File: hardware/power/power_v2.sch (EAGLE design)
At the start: 67 parts, among them J1 12v, J100 FASTON1289_ST, J101 FASTON1289_ST, J2 5v, J3 XT30PW-F, J4 XT30PW-F, J5 XT30PW-F, J6 XT30PW-F, J7 2-PIN, J8 2-PIN, Q1 PSMN1R0-40YSH, Q2 MMBT5401L, Q3 MMBT5401L, Q4 PSMN1R0-40YSH, U1 PDQ30-Q24-S12-D, U2 PDQ30-Q24-S5-D, U3 LM5069_DGS_10, U4 LM5069_DGS_10

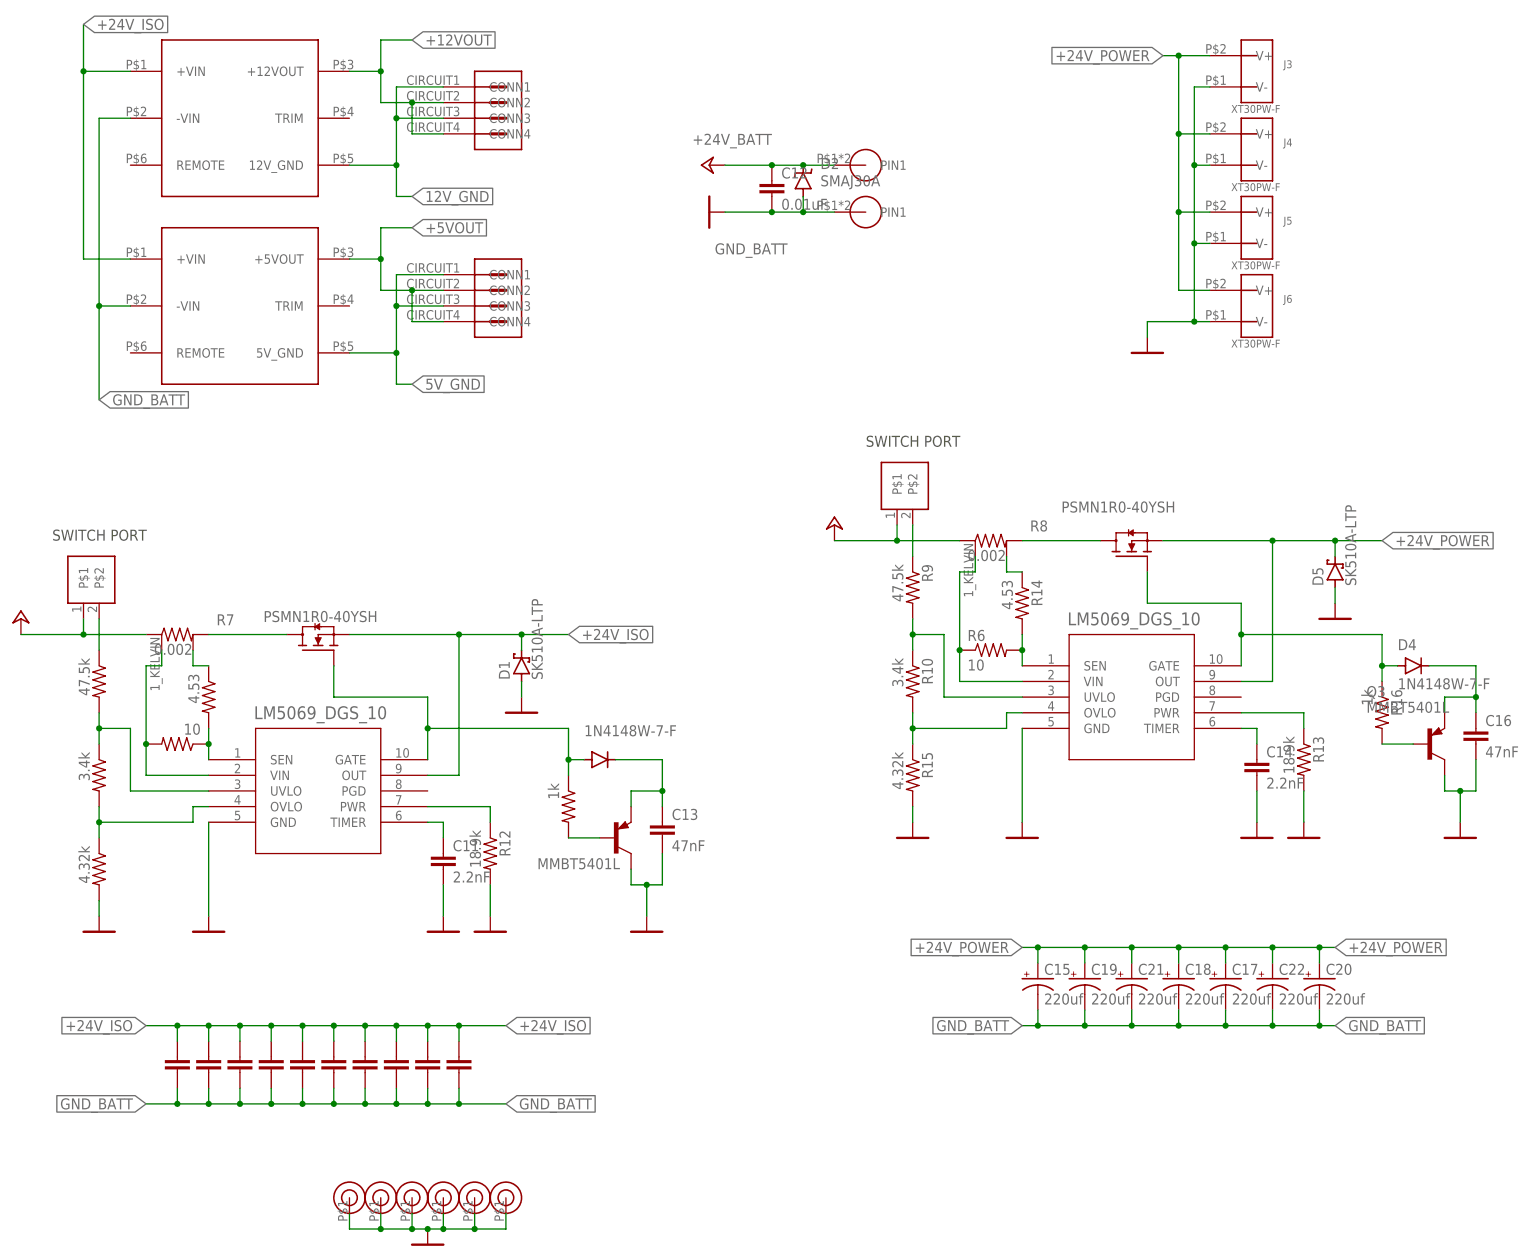
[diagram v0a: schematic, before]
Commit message: Chagned Rpwr
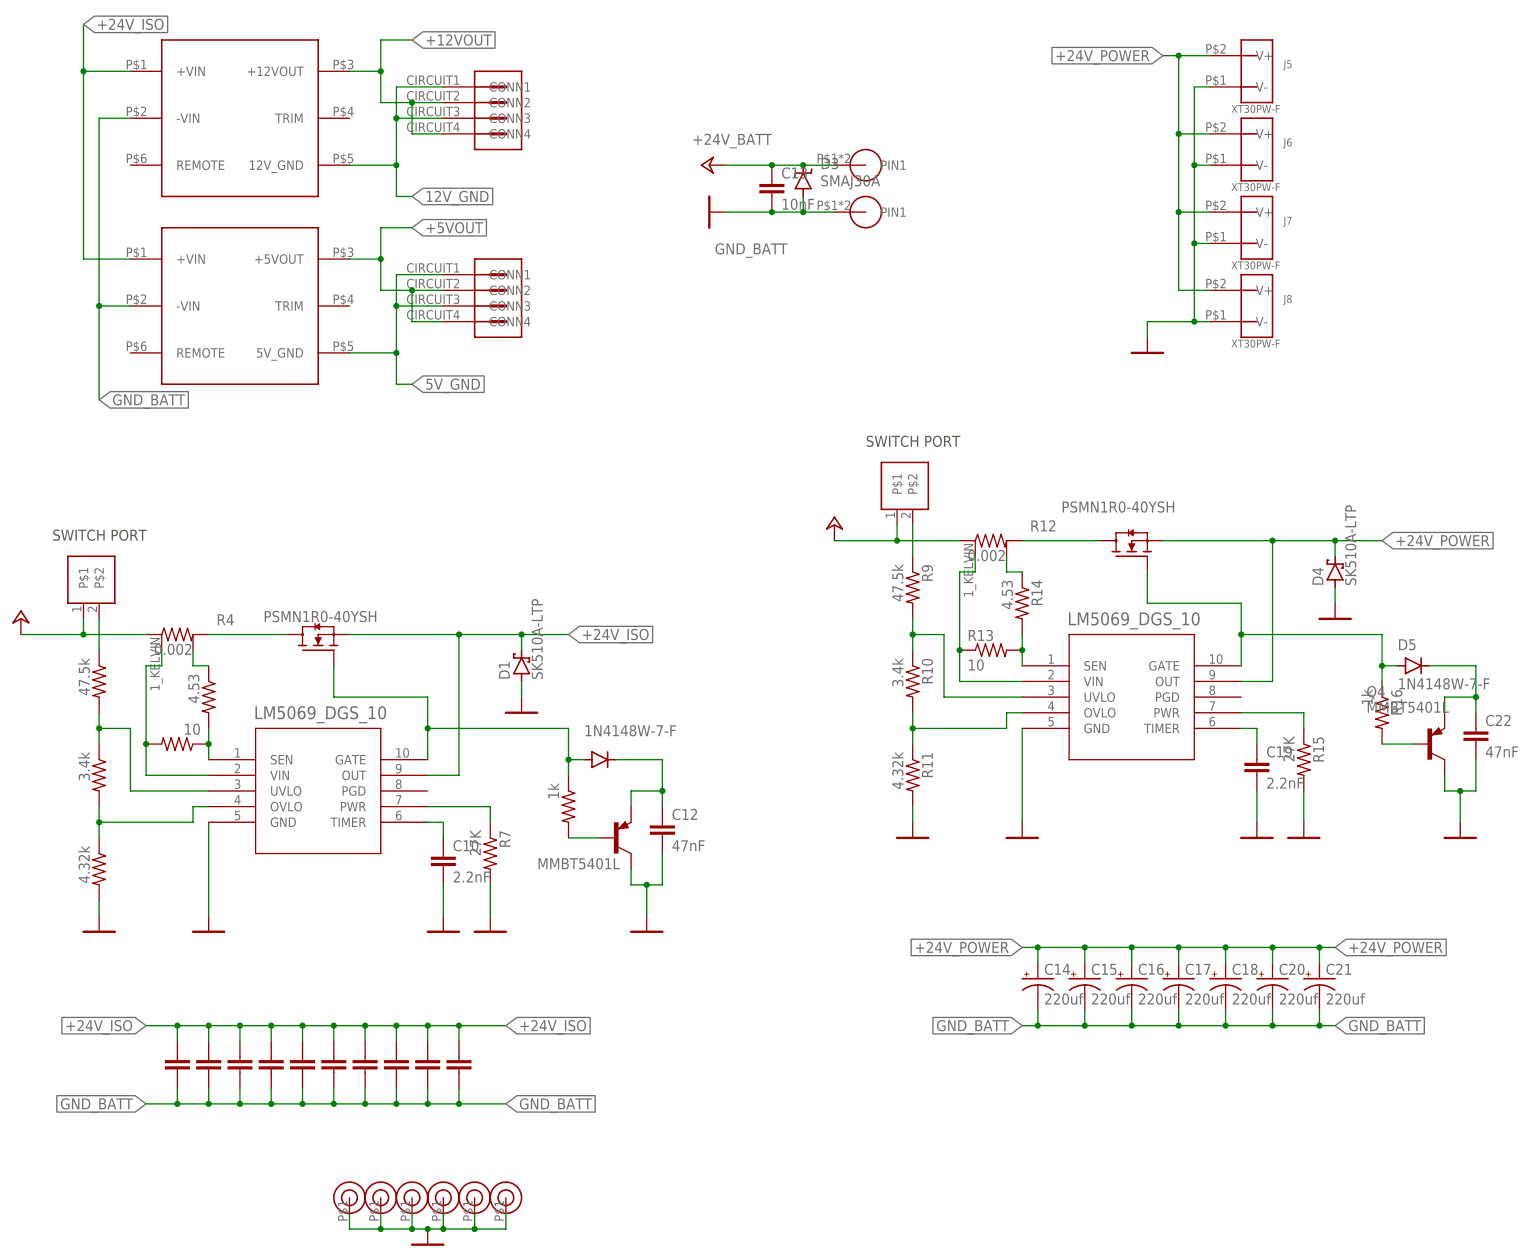
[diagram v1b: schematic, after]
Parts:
- removed U3, U4: LM5069_DGS_10, timlib:LM5069_DGS_10
- added PS3: PDQ30-Q24-S12-D, timlib:PDQ30-Q24-S12-D
- added PS4: PDQ30-Q24-S5-D, timlib:PDQ30-Q24-S5-D
- C1: value 10uF -> 2.2nF
- C10: value 10uF -> 2.2nF; device timlib:C_CERAMIC_1210 -> rcl:C-EUC0603
- C11: value 2.2nF -> 10uF; device rcl:C-EUC0603 -> timlib:C_CERAMIC_1210
- C12: value 0.01uF -> 47nF; device timlib:C_CERAMIC_1210 -> rcl:C-EUC0603
- C13: value 47nF -> 10nF
- C14: value 2.2nF -> 220uf; device rcl:C-EUC0603 -> timlib:35ZLH220MEFC8X11.5
- C16: value 47nF -> 220uf; device rcl:C-EUC0603 -> timlib:35ZLH220MEFC8X11.5
- C19: value 220uf -> 2.2nF; device timlib:35ZLH220MEFC8X11.5 -> rcl:C-EUC0603
- C22: value 220uf -> 47nF; device timlib:35ZLH220MEFC8X11.5 -> rcl:C-EUC0603
- C8: value 2.2nF -> 10uF
- D2: value SMAJ30A -> 1N4148W-7-F; device timlib:SMAJ30A -> timlib:1N4148W-7-F
- D3: value 1N4148W-7-F -> SMAJ30A; device timlib:1N4148W-7-F -> timlib:SMAJ30A
- D4: value 1N4148W-7-F -> SK510A-LTP; device timlib:1N4148W-7-F -> timlib:SK510A-LTP
- D5: value SK510A-LTP -> 1N4148W-7-F; device timlib:SK510A-LTP -> timlib:1N4148W-7-F
- J1: value 12v -> 2-PIN; device timlib:MOLEX_4_RA -> timlib:2-PIN
- J2: value 5v -> 12v
- J3: value XT30PW-F -> 5v; device timlib:XT30PW-F -> timlib:MOLEX_4_RA
- J4: value XT30PW-F -> 2-PIN; device timlib:XT30PW-F -> timlib:2-PIN
- J7, J8: value 2-PIN -> XT30PW-F; device timlib:2-PIN -> timlib:XT30PW-F
- Q3: value MMBT5401L -> PSMN1R0-40YSH; device timlib:MMBT5401L -> timlib:PSMN1R0-40YSH
- Q4: value PSMN1R0-40YSH -> MMBT5401L; device timlib:PSMN1R0-40YSH -> timlib:MMBT5401L
- R1: value 4.32k -> 47.5k
- R11: value 1k -> 4.32k
- R12: value 18.9k -> 0.002; device rcl:R-US_R0603 -> timlib:PMR25HZPFV2L00
- R13: value 18.9k -> 10
- R15: value 4.32k -> 27K
- R3: value 47.5k -> 4.32k
- R4: value 4.53 -> 0.002; device rcl:R-US_R0603 -> timlib:PMR25HZPFV2L00
- R6: value 10 -> 4.53
- R7: value 0.002 -> 27K; device timlib:PMR25HZPFV2L00 -> rcl:R-US_R0603
- R8: value 0.002 -> 1k; device timlib:PMR25HZPFV2L00 -> rcl:R-US_R0603
- U1: value PDQ30-Q24-S12-D -> LM5069_DGS_10; device timlib:PDQ30-Q24-S12-D -> timlib:LM5069_DGS_10
- U2: value PDQ30-Q24-S5-D -> LM5069_DGS_10; device timlib:PDQ30-Q24-S5-D -> timlib:LM5069_DGS_10
- renumbered J100 to P2, J101 to P1
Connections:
- net +12VOUT: now also J2.CONN2, J2.CONN4, PS3.+12VOUT; no longer J1.CONN2, J1.CONN4, U1.+12VOUT
- net +24V_BATT: now also C13.1, D3.C, J1.P$1, J4.P$1, R12.1, R4.1; no longer C12.1, D2.C, J7.P$1, J8.P$1, R7.1, R8.1
- net +24V_ISO: now also C11.1, PS3.+VIN, PS4.+VIN, U1.OUT; no longer C10.1, U1.+VIN, U2.+VIN, U4.OUT
- net +24V_POWER: now also C14.+, C16.+, D4.C, J7.V+, J8.V+, Q3.S, U2.OUT; no longer C19.+, C22.+, D5.C, J3.V+, J4.V+, Q4.S, U3.OUT
- net +5VOUT: now also J3.CONN2, J3.CONN4, PS4.+5VOUT; no longer J2.CONN2, J2.CONN4, U2.+5VOUT
- net 12V_GND: now also J2.CONN1, J2.CONN3, PS3.12V_GND; no longer J1.CONN1, J1.CONN3, U1.12V_GND
- net 5V_GND: now also J3.CONN1, J3.CONN3, PS4.5V_GND; no longer J2.CONN1, J2.CONN3, U2.5V_GND
- net GND_BATT: now also C14.-, C16.-, C19.2, C22.2, D3.A, D4.A, J7.V-, J8.V-, PS3.-VIN, PS4.-VIN, Q4.C, R11.2, R3.2, R7.2, U1.GND, U2.GND; no longer C14.2, C16.2, C19.-, C22.-, D2.A, D5.A, J3.V-, J4.V-, Q3.C, R1.2, R12.2, R13.2, U1.-VIN, U2.-VIN, U3.GND, U4.GND
- net MOSFET_DRAIN: now also Q3.D, R12.2; no longer Q4.D, R8.2
- net MOSFET_DRAIN1: now also R4.2; no longer R7.2
- net N$1: now also U2.UVLO; no longer U3.UVLO
- net N$10: now also R13.2, U2.SEN; no longer R6.2, U3.SEN
- net N$11: now also R12.2K; no longer R8.2K
- net N$12: now also R3.1, U1.OVLO; no longer R1.1, U4.OVLO
- net N$13: now also J1.P$2, R1.1; no longer J7.P$2, R3.1
- net N$14: now also D2.A, R8.1, U1.GATE; no longer D3.A, R11.1, U4.GATE
- net N$15: now also R7.1, U1.PWR; no longer R12.1, U4.PWR
- net N$16: now also C10.1, U1.TIMER; no longer C11.1, U4.TIMER
- net N$17: now also C12.1, D2.C; no longer C13.1, D3.C
- net N$18: now also R8.2; no longer R11.2
- net N$19: now also R12.1K, R13.1, U2.VIN; no longer R6.1, R8.1K, U3.VIN
- net N$2: now also R11.1, U2.OVLO; no longer R15.1, U3.OVLO
- net N$20: now also R6.2, U1.SEN; no longer R4.2, U4.SEN
- net N$21: now also R4.2K, R6.1; no longer R4.1, R7.2K
- net N$22: now also R4.1K, U1.VIN; no longer R7.1K, U4.VIN
- net N$3: now also J4.P$2; no longer J8.P$2
- net N$4: now also R1.2, U1.UVLO; no longer R3.2, U4.UVLO
- net N$5: now also D5.A, Q3.G, U2.GATE; no longer D4.A, Q4.G, U3.GATE
- net N$6: now also R15.1, U2.PWR; no longer R13.1, U3.PWR
- net N$7: now also C19.1, U2.TIMER; no longer C14.1, U3.TIMER
- net N$8: now also C22.1, D5.C, Q4.E; no longer C16.1, D4.C, Q3.E
- net N$9: now also Q4.B; no longer Q3.B
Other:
- moved on the sheet: C12, C13, C15, C17, C18, C20, C21, J5, J6, R13, R15

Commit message: Minor power updates
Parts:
- J1, J4: value 2-PIN -> LINEAR_2_JST_SH_RA; device timlib:2-PIN -> _T_conn:LINEAR_2_JST_SH_RA
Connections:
- net +24V_BATT: now also J1.P1, J4.P1; no longer J1.P$1, J4.P$1
- net N$13: now also J1.P2; no longer J1.P$2
- net N$3: now also J4.P2; no longer J4.P$2
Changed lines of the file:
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@@
 <?xml version="1.0" encoding="utf-8"?>
 <!DOCTYPE eagle SYSTEM "eagle.dtd">
-<eagle version="9.5.2">
+<eagle version="9.6.1">
 <drawing>
 <settings>
@@
 <part name="PS4" library="timlib" library_urn="urn:adsk.eagle:library:16152524" deviceset="PDQ30-Q24-S5-D" device="" package3d_urn="urn:adsk.eagle:package:16187995/4"/>
 <part name="PS3" library="timlib" library_urn="urn:adsk.eagle:library:16152524" deviceset="PDQ30-Q24-S12-D" device="" package3d_urn="urn:adsk.eagle:package:16187995/4"/>
-<part name="J4" library="timlib" library_urn="urn:adsk.eagle:library:16152524" deviceset="2-PIN" device="" package3d_urn="urn:adsk.eagle:package:16399492/4"/>
 <part name="C1" library="timlib" library_urn="urn:adsk.eagle:library:16152524" deviceset="C_CERAMIC" device="_1210" package3d_urn="urn:adsk.eagle:package:23619/2" value="2.2nF"/>
 <part name="C2" library="timlib" library_urn="urn:adsk.eagle:library:16152524" deviceset="C_CERAMIC" device="_1210" package3d_urn="urn:adsk.eagle:package:23619/2" value="10uF"/>
@@
 <part name="U$11" library="timlib" library_urn="urn:adsk.eagle:library:16152524" deviceset="BATT_GND" device="" value="GND_BATT"/>
 <part name="U$12" library="timlib" library_urn="urn:adsk.eagle:library:16152524" deviceset="BATT_GND" device="" value="GND_BATT"/>
-<part name="J1" library="timlib" library_urn="urn:adsk.eagle:library:16152524" deviceset="2-PIN" device="" package3d_urn="urn:adsk.eagle:package:16399492/4"/>
 <part name="U1" library="timlib" library_urn="urn:adsk.eagle:library:16152524" deviceset="LM5069_DGS_10" device="" package3d_urn="urn:adsk.eagle:package:16499421/3"/>
 <part name="P+4" library="timlib" library_urn="urn:adsk.eagle:library:16152524" deviceset="V_BATT" device="" value="+24V_BATT"/>
@@
 <part name="R4" library="timlib" library_urn="urn:adsk.eagle:library:16152524" deviceset="PMR25HZPFV" device="2L00" package3d_urn="urn:adsk.eagle:package:16502583/3" value="0.002"/>
 <part name="R12" library="timlib" library_urn="urn:adsk.eagle:library:16152524" deviceset="PMR25HZPFV" device="2L00" package3d_urn="urn:adsk.eagle:package:16502583/3" value="0.002"/>
-<part name="H1" library="timlib" library_urn="urn:adsk.eagle:library:16152524" deviceset="GND_HOLE" device="_M3" package3d_urn="urn:adsk.eagle:package:19295484/2"/>
-<part name="H2" library="timlib" library_urn="urn:adsk.eagle:library:16152524" deviceset="GND_HOLE" device="_M3" package3d_urn="urn:adsk.eagle:package:19295484/2"/>
-<part name="H3" library="timlib" library_urn="urn:adsk.eagle:library:16152524" deviceset="GND_HOLE" device="_M3" package3d_urn="urn:adsk.eagle:package:19295484/2"/>
-<part name="H4" library="timlib" library_urn="urn:adsk.eagle:library:16152524" deviceset="GND_HOLE" device="_M3" package3d_urn="urn:adsk.eagle:package:19295484/2"/>
-<part name="H5" library="timlib" library_urn="urn:adsk.eagle:library:16152524" deviceset="GND_HOLE" device="_M3" package3d_urn="urn:adsk.eagle:package:19295484/2"/>
-<part name="H6" library="timlib" library_urn="urn:adsk.eagle:library:16152524" deviceset="GND_HOLE" device="_M3" package3d_urn="urn:adsk.eagle:package:19295484/2"/>
+<part name="H1" library="timlib" library_urn="urn:adsk.eagle:library:16152524" deviceset="GND_HOLE" device="_M3" package3d_urn="urn:adsk.eagle:package:19295484/3"/>
+<part name="H2" library="timlib" library_urn="urn:adsk.eagle:library:16152524" deviceset="GND_HOLE" device="_M3" package3d_urn="urn:adsk.eagle:package:19295484/3"/>
+<part name="H3" library="timlib" library_urn="urn:adsk.eagle:library:16152524" deviceset="GND_HOLE" device="_M3" package3d_urn="urn:adsk.eagle:package:19295484/3"/>
+<part name="H4" library="timlib" library_urn="urn:adsk.eagle:library:16152524" deviceset="GND_HOLE" device="_M3" package3d_urn="urn:adsk.eagle:package:19295484/3"/>
+<part name="H5" library="timlib" library_urn="urn:adsk.eagle:library:16152524" deviceset="GND_HOLE" device="_M3" package3d_urn="urn:adsk.eagle:package:19295484/3"/>
+<part name="H6" library="timlib" library_urn="urn:adsk.eagle:library:16152524" deviceset="GND_HOLE" device="_M3" package3d_urn="urn:adsk.eagle:package:19295484/3"/>
 <part name="U$24" library="timlib" library_urn="urn:adsk.eagle:library:16152524" deviceset="BATT_GND" device="" value="GND_BATT"/>
 <part name="C10" library="rcl" library_urn="urn:adsk.eagle:library:334" deviceset="C-EU" device="C0603" package3d_urn="urn:adsk.eagle:package:23616/2" value="2.2nF"/>
@@
 <part name="C12" library="rcl" library_urn="urn:adsk.eagle:library:334" deviceset="C-EU" device="C0603" package3d_urn="urn:adsk.eagle:package:23616/2" value="47nF"/>
 <part name="C22" library="rcl" library_urn="urn:adsk.eagle:library:334" deviceset="C-EU" device="C0603" package3d_urn="urn:adsk.eagle:package:23616/2" value="47nF"/>
+<part name="J1" library="_T_conn" library_urn="urn:adsk.eagle:library:19570503" deviceset="LINEAR_2" device="_JST_SH_RA" package3d_urn="urn:adsk.eagle:package:19570552/2"/>
+<part name="J4" library="_T_conn" library_urn="urn:adsk.eagle:library:19570503" deviceset="LINEAR_2" device="_JST_SH_RA" package3d_urn="urn:adsk.eagle:package:19570552/2"/>
 </parts>
 <sheets>
@@
 </instance>
 <instance part="U$12" gate="G$1" x="200.66" y="152.4" smashed="yes" grouprefs="24V_POWER"/>
-<instance part="J4" gate="G$1" x="162.56" y="124.46" smashed="yes" rot="R90" grouprefs="24V_SOFTSTART"/>
 <instance part="U2" gate="A" x="198.12" y="93.98" smashed="yes" grouprefs="24V_SOFTSTART">
 <attribute name="VALUE" x="187.6806" y="105.6386" size="2.0828" layer="96" ratio="6" rot="SR0"/>
@@
 <instance part="C9" gate="G$1" x="83.82" y="35.56" smashed="yes" grouprefs="ISO_DECOUPLE"/>
 <instance part="C11" gate="G$1" x="88.9" y="35.56" smashed="yes" grouprefs="ISO_DECOUPLE"/>
-<instance part="J1" gate="G$1" x="30.48" y="109.22" smashed="yes" rot="R90" grouprefs="ISO_SOFTSTART"/>
 <instance part="U1" gate="A" x="66.04" y="78.74" smashed="yes" grouprefs="ISO_SOFTSTART">
 <attribute name="VALUE" x="55.6006" y="90.3986" size="2.0828" layer="96" ratio="6" rot="SR0"/>
@@
 <attribute name="VALUE" x="255.524" y="84.201" size="1.778" layer="96"/>
 </instance>
+<instance part="J1" gate="G$1" x="27.94" y="111.76" smashed="yes" rot="R90">
+<attribute name="NAME" x="25.146" y="109.22" size="1.778" layer="95" rot="R90"/>
+<attribute name="VALUE" x="35.56" y="109.22" size="1.778" layer="96" rot="R90"/>
+</instance>
+<instance part="J4" gate="G$1" x="160.02" y="127" smashed="yes" rot="R90">
+<attribute name="NAME" x="157.226" y="124.46" size="1.778" layer="95" rot="R90"/>
+<attribute name="VALUE" x="167.64" y="124.46" size="1.778" layer="96" rot="R90"/>
+</instance>
 </instances>
 <busses>
@@
 <wire x1="170.18" y1="119.38" x2="160.02" y2="119.38" width="0.1524" layer="91" grouprefs="24V_SOFTSTART"/>
 <wire x1="160.02" y1="119.38" x2="149.86" y2="119.38" width="0.1524" layer="91" grouprefs="24V_SOFTSTART"/>
-<pinref part="J4" gate="G$1" pin="P$1"/>
 <wire x1="160.02" y1="121.92" x2="160.02" y2="119.38" width="0.1524" layer="91" grouprefs="24V_SOFTSTART"/>
 <junction x="160.02" y="119.38" grouprefs="24V_SOFTSTART"/>
 <pinref part="R12" gate="G$1" pin="1"/>
+<pinref part="J4" gate="G$1" pin="P1"/>
 </segment>
 <segment>
@@
 <wire x1="27.94" y1="106.68" x2="27.94" y2="104.14" width="0.1524" layer="91" grouprefs="ISO_SOFTSTART"/>
 <junction x="27.94" y="104.14" grouprefs="ISO_SOFTSTART"/>
-<pinref part="J1" gate="G$1" pin="P$1"/>
 <pinref part="P+4" gate="1" pin="+24V"/>
 <pinref part="R4" gate="G$1" pin="1"/>
+<pinref part="J1" gate="G$1" pin="P1"/>
 </segment>
 </net>
@@
 <net name="N$3" class="0">
 <segment>
-<pinref part="J4" gate="G$1" pin="P$2"/>
 <pinref part="R9" gate="G$1" pin="1"/>
 <wire x1="162.56" y1="121.92" x2="162.56" y2="116.84" width="0.1524" layer="91" grouprefs="24V_SOFTSTART"/>
+<pinref part="J4" gate="G$1" pin="P2"/>
 </segment>
 </net>
@@
 <segment>
 <wire x1="30.48" y1="106.68" x2="30.48" y2="101.6" width="0.1524" layer="91" grouprefs="ISO_SOFTSTART"/>
-<pinref part="J1" gate="G$1" pin="P$2"/>
 <pinref part="R1" gate="G$1" pin="1"/>
-</segment>
-</net>
+<pinref part="J1" gate="G$1" pin="P2"/>
+</segment>
+</net>
